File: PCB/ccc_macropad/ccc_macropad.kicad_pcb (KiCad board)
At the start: 2 copper layers, 14 parts, among them SW1 SW_Push, SW2 SW_Push, SW3 SW_Push, SW4 SW_Push, SW5 SW_Push, SW6 SW_Push, U1 XIAO-RP2040-DIP

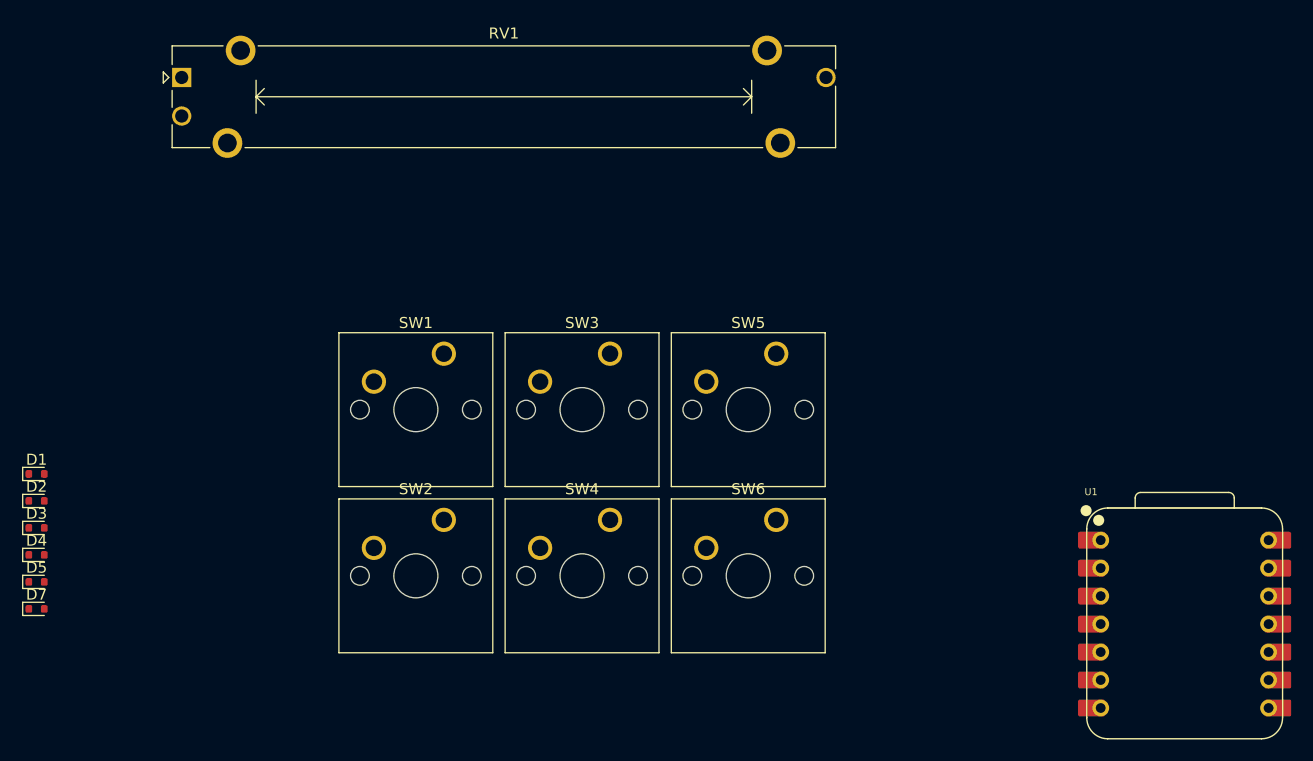
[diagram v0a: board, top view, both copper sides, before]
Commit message: feat: create and include all footprint. import all components in PCB
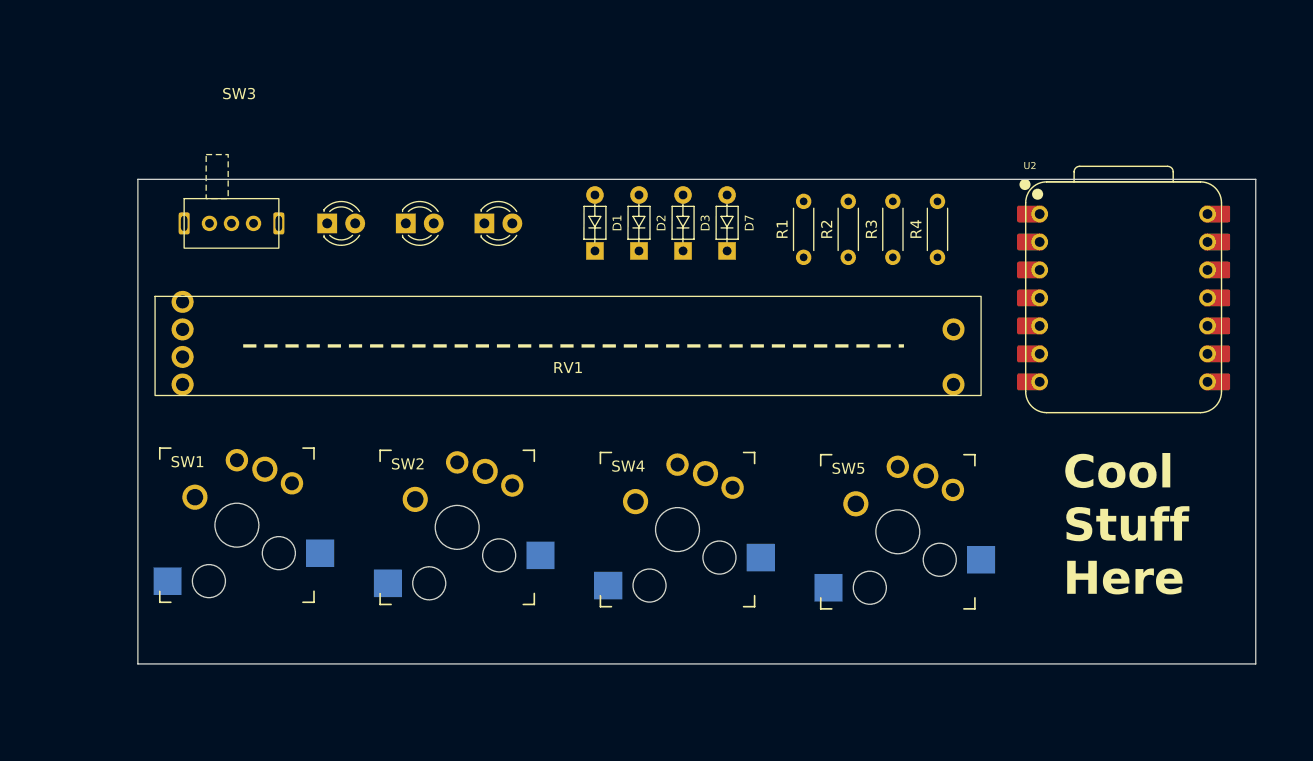
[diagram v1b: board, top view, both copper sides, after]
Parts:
- removed D4, D5: 1N4148WT, Diode_SMD:D_SOD-523
- removed SW6: SW_Push, Button_Switch_Keyboard:SW_Cherry_MX_1.00u_PCB
- removed U1: XIAO-RP2040-DIP, XIAO Seeduino:XIAO-RP2040-DIP
- added D6: LED, LED_THT:LED_D3.0mm, F.Cu at (127.7, 42.0)
- added D8: LED, LED_THT:LED_D3.0mm, F.Cu at (142.0, 42.0)
- added D9: LED, LED_THT:LED_D3.0mm, F.Cu at (134.8, 42.0)
- added R1: 100R, Resistor_THT:R_Axial_DIN0204_L3.6mm_D1.6mm_P5.08mm_Horizontal, F.Cu at (170.9, 45.1)
- added R2: 100R, Resistor_THT:R_Axial_DIN0204_L3.6mm_D1.6mm_P5.08mm_Horizontal, F.Cu at (175.0, 45.1)
- added R3: 100R, Resistor_THT:R_Axial_DIN0204_L3.6mm_D1.6mm_P5.08mm_Horizontal, F.Cu at (179.1, 45.1)
- added R4: 10k, Resistor_THT:R_Axial_DIN0204_L3.6mm_D1.6mm_P5.08mm_Horizontal, F.Cu at (183.1, 45.1)
- added U2: XIAO-RP2040-DIP, XIAO Seeduino:XIAO-RP2040-DIP, F.Cu at (200.0, 48.8)
- D1, D2, D3, D7: footprint Diode_SMD:D_SOD-523 -> Key_Switches:D_DO-35_SOD27_P5.08mm_Horizontal
- RV1: value Analogue_input_slider -> Analogue_input_slider 10k; footprint Potentiometer_THT:Potentiometer_Bourns_PTA4543_Single_Slide -> CustomFootprints:Potentiometer_slide_75mm_range_60mm_2_sets
- SW1, SW2, SW4, SW5: footprint Button_Switch_Keyboard:SW_Cherry_MX_1.00u_PCB -> Key_Switches:Kailh_socket_MX_PG1350_optional
- SW3: value SW_Push -> OS/Left_Right-hand_Switch; footprint Button_Switch_Keyboard:SW_Cherry_MX_1.00u_PCB -> CustomFootprints:SPDT_3pin_2_pos_1P2T_tht_2.54mm_switch_sk12d07
- moved D7 70.0 mm to (164.0, 45.8), turned to 90 degrees
- moved D3 63.4 mm to (160.0, 45.8), turned to 90 degrees
- moved D2 58.7 mm to (156.0, 45.8), turned to 90 degrees
- moved D1 54.1 mm to (152.0, 45.8), turned to 90 degrees
- moved SW3 41.2 mm to (114.7, 39.8)
- moved RV1 29.0 mm to (112.1, 57.6)
- moved SW1 24.4 mm to (119.5, 69.4)
- moved SW5 19.6 mm to (179.5, 70.0)
- moved SW4 6.19 mm to (159.5, 69.8)
- moved SW2 1.39 mm to (139.5, 69.6)
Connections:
- RV1 pad 1: Net-(U1-GND) -> GND
- SW2 pad 1: Net-(D1-K) -> Net-(U2-GPIO4/MISO)
- SW5 pad 1: Net-(D1-K) -> Net-(U2-GPIO4/MISO)
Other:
- board outline added: 101.5 x 44 mm
- board text added: "Cool Stuff Here"
- board text added: "K"

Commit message: pcb:routing
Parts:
- moved D7 12.7 mm to (153.5, 38.6), turned to -90 degrees
- moved R4 12.1 mm to (171.0, 45.0)
- moved D1 11.9 mm to (161.5, 38.6), turned to -90 degrees
- moved D2 11.9 mm to (165.5, 38.6), turned to -90 degrees
- moved D3 7.55 mm to (157.5, 38.6), turned to -90 degrees
- moved D9 4.71 mm to (139.4, 40.7), turned to -90 degrees
- moved D6 4.71 mm to (132.2, 40.7), turned to -90 degrees
- moved D8 4.71 mm to (146.5, 40.7), turned to -90 degrees
- moved R1 4.05 mm to (175.0, 45.1)
- moved R2 4.05 mm to (179.1, 45.1)
- moved R3 4.05 mm to (183.1, 45.1)
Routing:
- net Net-(U2-GPIO2/SCK): track 0.00 -> 143.8 mm
- net GND: track 0.00 -> 106.9 mm
- net Net-(SW3-B): track 0.00 -> 94.2 mm
- net Net-(U2-GPIO4/MISO): track 0.00 -> 92.8 mm
- net Net-(U2-GPIO26/ADC0/A0): track 0.00 -> 81.1 mm
- net Net-(SW3-C): track 0.00 -> 57.7 mm
- net Net-(D7-A): track 0.00 -> 55.7 mm
- net Net-(D1-K): track 0.00 -> 54.1 mm
- net Net-(U2-3V3): track 0.00 -> 46.9 mm
- net Net-(D6-A): track 0.00 -> 46.4 mm
- net Net-(D3-K): track 0.00 -> 45.7 mm
- net Net-(D9-A): track 0.00 -> 45.5 mm
- net Net-(D3-A): track 0.00 -> 40.2 mm
- net Net-(D2-A): track 0.00 -> 38.9 mm
- net Net-(D8-A): track 0.00 -> 33.9 mm
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
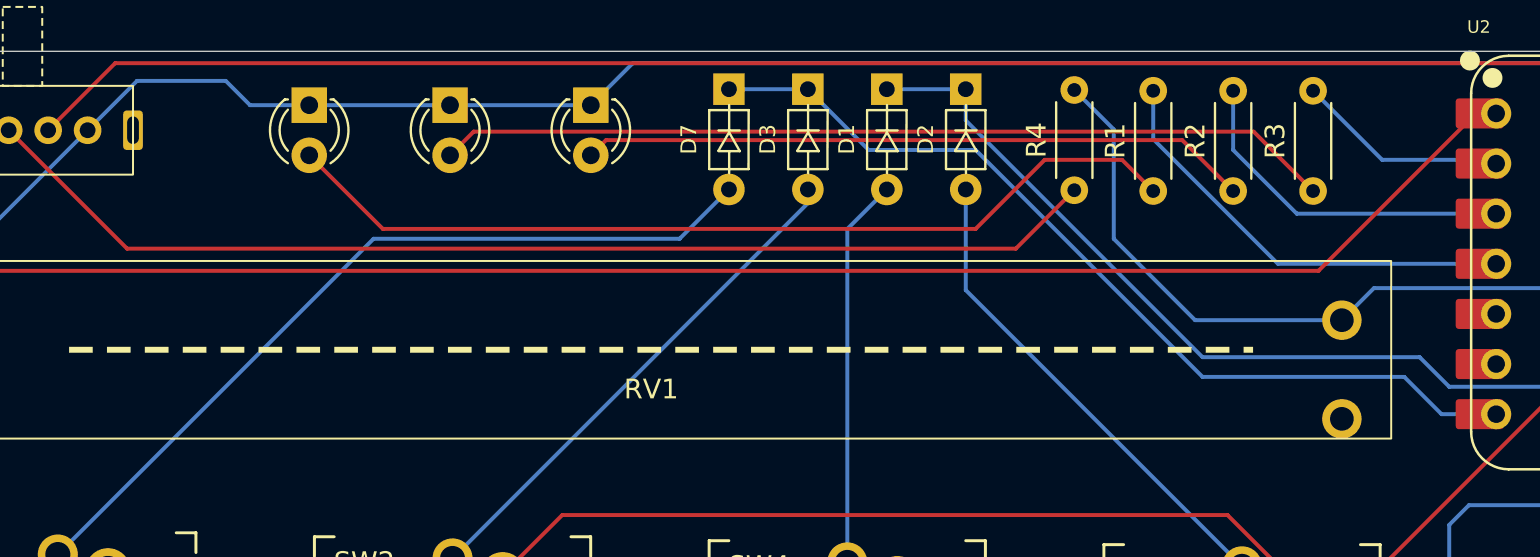
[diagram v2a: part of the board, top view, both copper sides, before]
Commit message: PCB:feat: update footprint slider
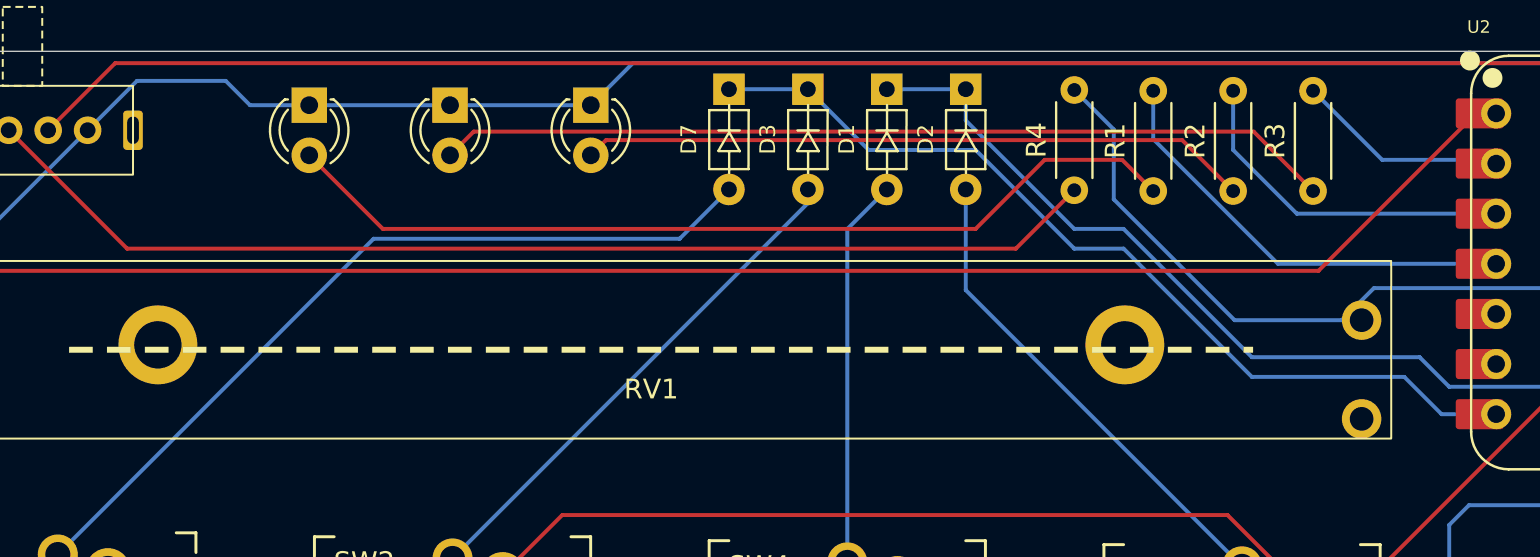
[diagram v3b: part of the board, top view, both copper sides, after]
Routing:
- net Net-(U2-3V3): track 46.9 -> 45.8 mm
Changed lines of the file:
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@@
 		)
 		(pad "3" thru_hole circle
-			(at 72.5 -6)
+			(at 73.5 -6)
 			(size 2 2)
 			(drill 1.2)
@@
 		)
 		(pad "3'" thru_hole circle
-			(at 72.5 -1)
+			(at 73.5 -1)
 			(size 2 2)
 			(drill 1.2)
@@
 			(remove_unused_layers no)
 		)
+		(pad "MP" thru_hole circle
+			(at 12.5 -4.75)
+			(size 4 4)
+			(drill 2.4)
+			(layers "*.Cu" "*.Mask")
+			(remove_unused_layers no)
+		)
+		(pad "MP" thru_hole circle
+			(at 61.5 -4.75)
+			(size 4 4)
+			(drill 2.4)
+			(layers "*.Cu" "*.Mask")
+			(remove_unused_layers no)
+		)
 		(embedded_fonts no)
 	)
@@
 	)
 	(segment
-		(start 177.5 53.5)
-		(end 188.5 53.5)
+		(start 190 55)
+		(end 197.5 55)
 		(width 0.2)
 		(layer "B.Cu")
@@
 	)
 	(segment
-		(start 161.5 39.92)
-		(end 165.5 39.92)
+		(start 180 53.5)
+		(end 188.5 53.5)
 		(width 0.2)
 		(layer "B.Cu")
@@
 	)
 	(segment
-		(start 188.5 53.5)
-		(end 190 55)
+		(start 165.5 41.5)
+		(end 171 47)
 		(width 0.2)
 		(layer "B.Cu")
@@
 	)
 	(segment
-		(start 190 55)
-		(end 197.5 55)
+		(start 173.5 47)
+		(end 180 53.5)
 		(width 0.2)
 		(layer "B.Cu")
@@
 	)
 	(segment
-		(start 198.99481 56.5)
-		(end 199 56.5)
+		(start 161.5 39.92)
+		(end 165.5 39.92)
 		(width 0.2)
 		(layer "B.Cu")
@@
 	)
 	(segment
+		(start 198.99481 56.5)
+		(end 199 56.5)
+		(width 0.2)
+		(layer "B.Cu")
+		(net 2)
+	)
+	(segment
 		(start 199 56.5)
 		(end 207.798 56.5)
@@
 	)
 	(segment
-		(start 165.5 41.5)
-		(end 177.5 53.5)
+		(start 171 47)
+		(end 173.5 47)
+		(width 0.2)
+		(layer "B.Cu")
+		(net 2)
+	)
+	(segment
+		(start 188.5 53.5)
+		(end 190 55)
 		(width 0.2)
 		(layer "B.Cu")
@@
 	)
 	(segment
-		(start 187.723 54.5)
-		(end 189.6115 56.3885)
+		(start 171 48)
+		(end 173.5 48)
 		(width 0.2)
 		(layer "B.Cu")
@@
 	)
 	(segment
-		(start 177.5 54.5)
+		(start 157.5 39.92)
+		(end 160.58 43)
+		(width 0.2)
+		(layer "B.Cu")
+		(net 4)
+	)
+	(segment
+		(start 180 54.5)
 		(end 187.723 54.5)
 		(width 0.2)
@@
 	)
 	(segment
-		(start 157.5 39.92)
-		(end 160.58 43)
+		(start 187.723 54.5)
+		(end 189.6115 56.3885)
 		(width 0.2)
 		(layer "B.Cu")
@@
 	)
 	(segment
-		(start 160.58 43)
-		(end 166 43)
+		(start 189.6115 56.3885)
+		(end 192.38 56.3885)
 		(width 0.2)
 		(layer "B.Cu")
@@
 	(segment
 		(start 166 43)
-		(end 177.5 54.5)
+		(end 171 48)
+		(width 0.2)
+		(layer "B.Cu")
+		(net 4)
+	)
+	(segment
+		(start 160.58 43)
+		(end 166 43)
 		(width 0.2)
 		(layer "B.Cu")
@@
 	)
 	(segment
-		(start 189.6115 56.3885)
-		(end 192.38 56.3885)
+		(start 173.5 48)
+		(end 180 54.5)
 		(width 0.2)
 		(layer "B.Cu")
@@
 	)
 	(segment
-		(start 177.125 51.625)
+		(start 179.125 51.625)
 		(end 184.56 51.625)
 		(width 0.2)
@@
 	)
 	(segment
-		(start 203.8485 50)
-		(end 207.62 46.2285)
+		(start 173 41.96)
+		(end 173 45.5)
 		(width 0.2)
 		(layer "B.Cu")
@@
 	)
 	(segment
-		(start 173 47.5)
-		(end 177.125 51.625)
+		(start 173 45.5)
+		(end 179.125 51.625)
 		(width 0.2)
 		(layer "B.Cu")
@@
 	)
 	(segment
-		(start 184.56 51.625)
-		(end 186.185 50)
+		(start 203.8485 50)
+		(end 207.62 46.2285)
 		(width 0.2)
 		(layer "B.Cu")
@@
 	)
 	(segment
-		(start 173 41.96)
-		(end 173 47.5)
+		(start 186.185 50)
+		(end 203.8485 50)
 		(width 0.2)
 		(layer "B.Cu")
@@
 	)
 	(segment
-		(start 186.185 50)
-		(end 203.8485 50)
+		(start 184.56 51.625)
+		(end 186.185 50)
 		(width 0.2)
 		(layer "B.Cu")

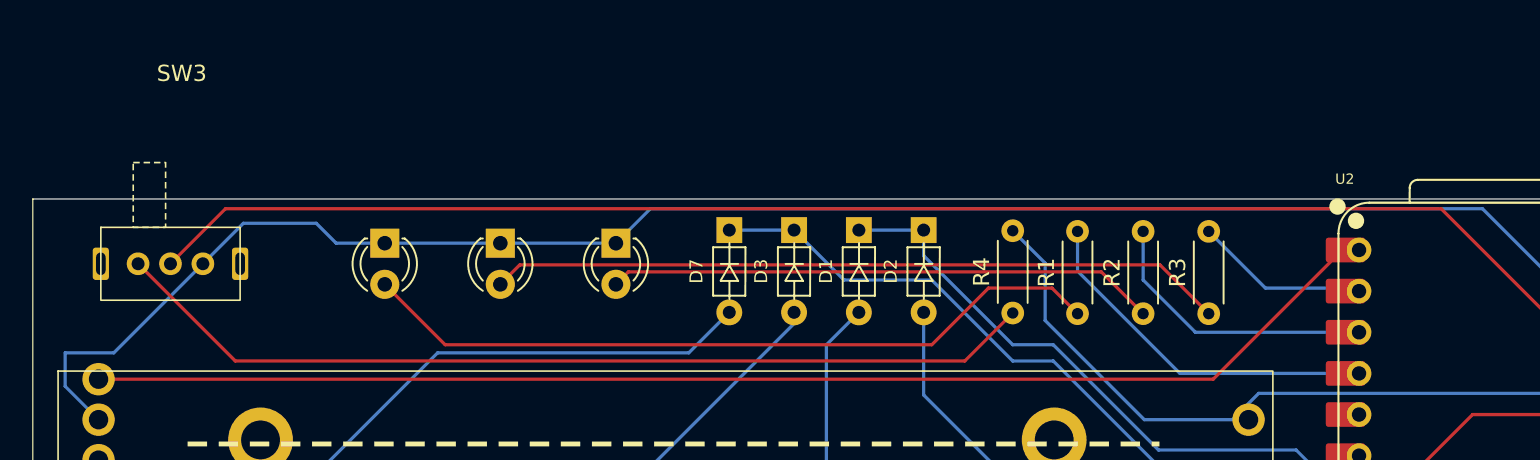
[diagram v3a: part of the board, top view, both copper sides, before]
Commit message: PCB:feat: update footprint spdt switch
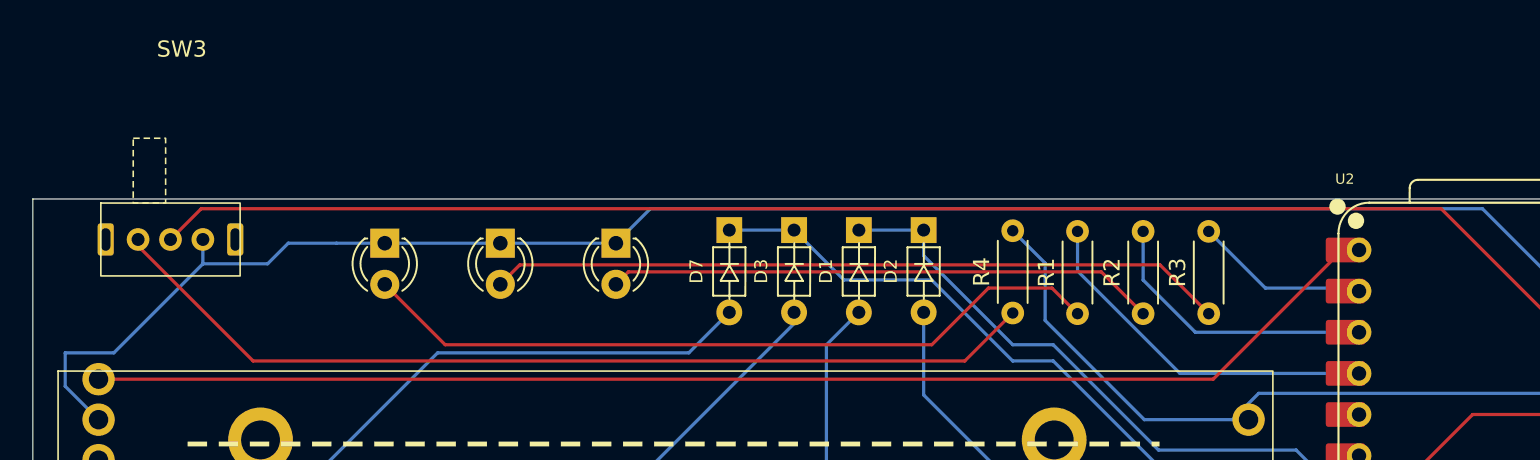
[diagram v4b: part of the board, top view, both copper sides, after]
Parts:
- moved SW3 1.50 mm to (114.7, 38.2)
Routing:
- net Net-(SW3-C): track 57.7 -> 58.6 mm
- net Net-(SW3-B): track 94.2 -> 93.6 mm
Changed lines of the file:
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@@
 	(footprint "CustomFootprints:SPDT_3pin_2_pos_1P2T_tht_2.54mm_switch_sk12d07"
 		(layer "F.Cu")
-		(at 114.7 39.75)
+		(at 114.7 38.25)
 		(property "Reference" "SW3"
 			(at 5 -9.5 0)
@@
 		)
 		(pad "MH" thru_hole roundrect
-			(at 0 2.25)
+			(at 0.3 2.25)
 			(size 1 2)
 			(drill oval 0.6 1.4)
@@
 		)
 		(pad "MH" thru_hole roundrect
-			(at 8.6 2.25)
+			(at 8.3 2.25)
 			(size 1 2)
 			(drill oval 0.6 1.4)
@@
 	)
 	(segment
-		(start 200 38.601)
-		(end 205.0875 43.6885)
+		(start 125 42)
+		(end 121 42)
 		(width 0.2)
 		(layer "B.Cu")
@@
 	)
 	(segment
-		(start 139.365 40.73)
-		(end 146.5 40.73)
+		(start 121 42)
+		(end 121 40.5)
 		(width 0.2)
 		(layer "B.Cu")
@@
 	)
 	(segment
-		(start 115.5 47.5)
-		(end 121 42)
+		(start 200 38.601)
+		(end 205.0875 43.6885)
 		(width 0.2)
 		(layer "B.Cu")
@@
 	)
 	(segment
-		(start 148.629 38.601)
-		(end 200 38.601)
+		(start 126.27 40.73)
+		(end 125 42)
 		(width 0.2)
 		(layer "B.Cu")
@@
 	)
 	(segment
-		(start 112.5 49.565)
-		(end 112.5 47.5)
+		(start 129.23 40.73)
+		(end 126.27 40.73)
 		(width 0.2)
 		(layer "B.Cu")
@@
 	)
 	(segment
-		(start 132.23 40.73)
-		(end 139.365 40.73)
+		(start 139.365 40.73)
+		(end 146.5 40.73)
+		(width 0.2)
+		(layer "B.Cu")
+		(net 8)
+	)
+	(segment
+		(start 115.5 47.5)
+		(end 121 42)
 		(width 0.2)
 		(layer "B.Cu")
@@
 	)
 	(segment
-		(start 128 39.5)
-		(end 129.23 40.73)
+		(start 148.629 38.601)
+		(end 200 38.601)
 		(width 0.2)
 		(layer "B.Cu")
@@
 	)
 	(segment
-		(start 123.5 39.5)
-		(end 128 39.5)
+		(start 112.5 49.565)
+		(end 112.5 47.5)
 		(width 0.2)
 		(layer "B.Cu")
@@
 	)
 	(segment
-		(start 121 42)
-		(end 123.5 39.5)
+		(start 132.23 40.73)
+		(end 139.365 40.73)
 		(width 0.2)
 		(layer "B.Cu")
@@
 	)
 	(segment
-		(start 123 48)
-		(end 117 42)
+		(start 117 40.898834)
+		(end 117 40.5)
 		(width 0.2)
 		(layer "F.Cu")
@@
 	(segment
 		(start 168.04 48)
-		(end 123 48)
+		(end 124.101166 48)
 		(width 0.2)
 		(layer "F.Cu")
@@
 	)
 	(segment
-		(start 122.399 38.601)
-		(end 197.4525 38.601)
+		(start 124.101166 48)
+		(end 117 40.898834)
+		(width 0.2)
+		(layer "F.Cu")
+		(net 11)
+	)
+	(segment
+		(start 119 40.5)
+		(end 120.899 38.601)
 		(width 0.2)
 		(layer "F.Cu")
@@
 	)
 	(segment
-		(start 119 42)
-		(end 122.399 38.601)
+		(start 120.899 38.601)
+		(end 197.4525 38.601)
 		(width 0.2)
 		(layer "F.Cu")

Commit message: chores: font / fontsize
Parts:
- renumbered R2 to 100R, R3 to 100R, R1 to 100R, R4 to 10k

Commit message: PCB:feat: add ground plane / add mounting holes / route thickness .4mm
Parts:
- D6 LED: renamed from D6
- D8 LED: renamed from D8
- D9 LED: renamed from D9
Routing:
- net GND: track 107.4 -> 0.00 mm
- net Net-(SW3-B): track 93.6 -> 99.6 mm, vias 0 -> 1
- net Net-(D3-A): track 40.2 -> 45.7 mm
- net Net-(D7-A): track 55.7 -> 61.2 mm
- net Net-(D2-A): track 38.9 -> 43.2 mm
- net Net-(D9-A): track 45.5 -> 49.2 mm
- net Net-(D1-A): track 33.7 -> 37.1 mm
- net Net-(U2-GPIO4/MISO): track 92.8 -> 95.9 mm
- net Net-(SW3-C): track 58.6 -> 60.3 mm
- net Net-(U2-GPIO26/ADC0/A0): track 81.1 -> 82.8 mm
- net Net-(U2-GPIO27/ADC1/A1): track 10.8 -> 11.9 mm
- net Net-(U2-3V3): track 45.8 -> 44.8 mm
- net Net-(U2-GPIO2/SCK): track 143.8 -> 144.8 mm
- added copper zone on B.Cu, net GND
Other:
- outline, holes or cut-outs redrawn
- board text added: "+"
- board text added: "-"
- board text removed: "K"
